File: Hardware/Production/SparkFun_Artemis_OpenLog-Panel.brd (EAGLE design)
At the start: 137.2 x 168.9 mm, 2070 parts, among them J100 CORTEX_JTAG, J107 MICRO-SD, J109 CORTEX_JTAG, J116 MICRO-SD, J118 CORTEX_JTAG, J125 MICRO-SD, J127 CORTEX_JTAG, J134 MICRO-SD, J136 CORTEX_JTAG, J14 CORTEX_JTAG, J143 MICRO-SD, J17 MICRO-SD, J19 CORTEX_JTAG, J26 MICRO-SD, J28 CORTEX_JTAG, J35 MICRO-SD, J37 CORTEX_JTAG, J44 MICRO-SD, J46 CORTEX_JTAG, J53 MICRO-SD, J55 CORTEX_JTAG, J6 MICRO-SD, J62 MICRO-SD, J64 CORTEX_JTAG, J71 MICRO-SD, J73 CORTEX_JTAG, J8 CORTEX_JTAG, J80 MICRO-SD, J82 CORTEX_JTAG, J89 MICRO-SD, J91 CORTEX_JTAG, J98 MICRO-SD, Q1 20V/0.2A/8MHz/1.2Ω/1Vth, Q10 20V/0.2A/8MHz/1.2Ω/1Vth, Q11 20V/0.2A/8MHz/1.2Ω/1Vth, Q12 20V/4.2A/52mΩ/1.4W, Q13 20V/0.2A/8MHz/1.2Ω/1Vth, Q14 20V/0.2A/8MHz/1.2Ω/1Vth, Q15 20V/0.2A/8MHz/1.2Ω/1Vth, Q16 20V/0.2A/8MHz/1.2Ω/1Vth, Q17 20V/0.2A/8MHz/1.2Ω/1Vth, Q18 20V/4.2A/52mΩ/1.4W, Q19 20V/0.2A/8MHz/1.2Ω/1Vth, Q2 20V/4.2A/52mΩ/1.4W, Q20 20V/0.2A/8MHz/1.2Ω/1Vth, Q21 20V/0.2A/8MHz/1.2Ω/1Vth, Q22 20V/0.2A/8MHz/1.2Ω/1Vth, Q23 20V/0.2A/8MHz/1.2Ω/1Vth, Q24 20V/4.2A/52mΩ/1.4W, Q25 20V/0.2A/8MHz/1.2Ω/1Vth, Q26 20V/0.2A/8MHz/1.2Ω/1Vth, Q27 20V/0.2A/8MHz/1.2Ω/1Vth, Q28 20V/0.2A/8MHz/1.2Ω/1Vth, Q29 20V/0.2A/8MHz/1.2Ω/1Vth, Q3 20V/0.2A/8MHz/1.2Ω/1Vth, Q30 20V/4.2A/52mΩ/1.4W, Q31 20V/0.2A/8MHz/1.2Ω/1Vth, Q32 20V/0.2A/8MHz/1.2Ω/1Vth, Q33 20V/0.2A/8MHz/1.2Ω/1Vth, Q34 20V/0.2A/8MHz/1.2Ω/1Vth, Q35 20V/0.2A/8MHz/1.2Ω/1Vth, Q36 20V/4.2A/52mΩ/1.4W, Q37 20V/0.2A/8MHz/1.2Ω/1Vth, Q38 20V/0.2A/8MHz/1.2Ω/1Vth, Q39 20V/0.2A/8MHz/1.2Ω/1Vth, Q4 20V/0.2A/8MHz/1.2Ω/1Vth, Q40 20V/0.2A/8MHz/1.2Ω/1Vth, Q41 20V/0.2A/8MHz/1.2Ω/1Vth, Q42 20V/4.2A/52mΩ/1.4W, Q43 20V/0.2A/8MHz/1.2Ω/1Vth, Q44 20V/0.2A/8MHz/1.2Ω/1Vth, Q45 20V/0.2A/8MHz/1.2Ω/1Vth, Q46 20V/0.2A/8MHz/1.2Ω/1Vth, Q47 20V/0.2A/8MHz/1.2Ω/1Vth, Q48 20V/4.2A/52mΩ/1.4W, Q49 20V/0.2A/8MHz/1.2Ω/1Vth, Q5 20V/0.2A/8MHz/1.2Ω/1Vth, Q50 20V/0.2A/8MHz/1.2Ω/1Vth, Q51 20V/0.2A/8MHz/1.2Ω/1Vth, Q52 20V/0.2A/8MHz/1.2Ω/1Vth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

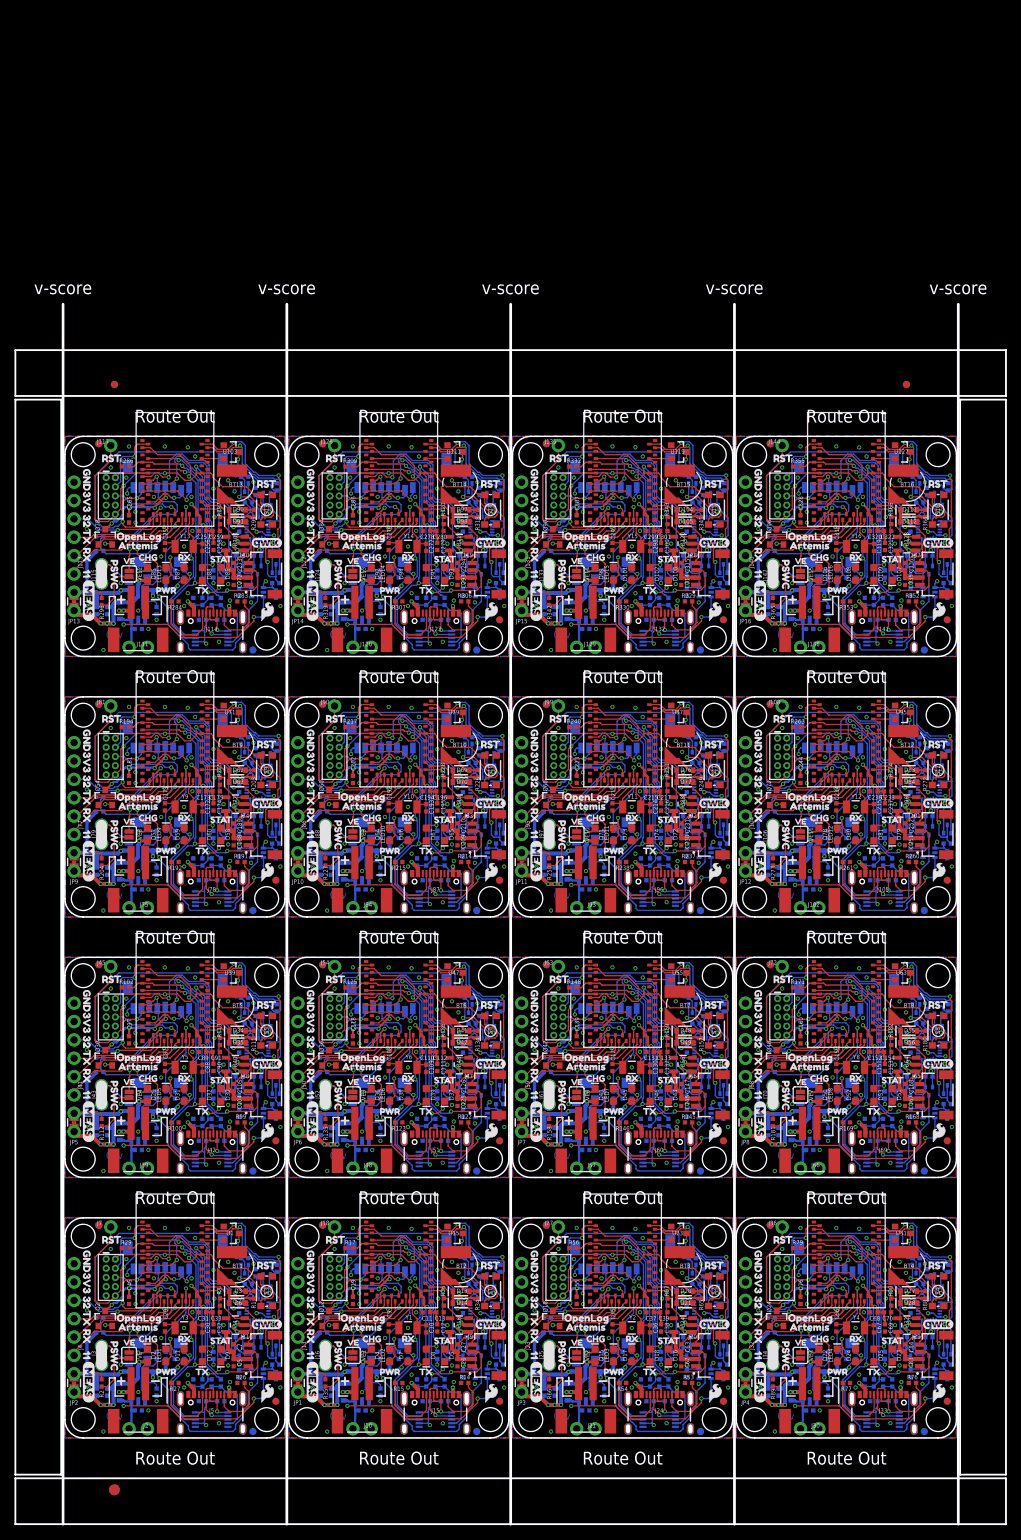
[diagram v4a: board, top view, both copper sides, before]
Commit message: Added revised production files (3x5)
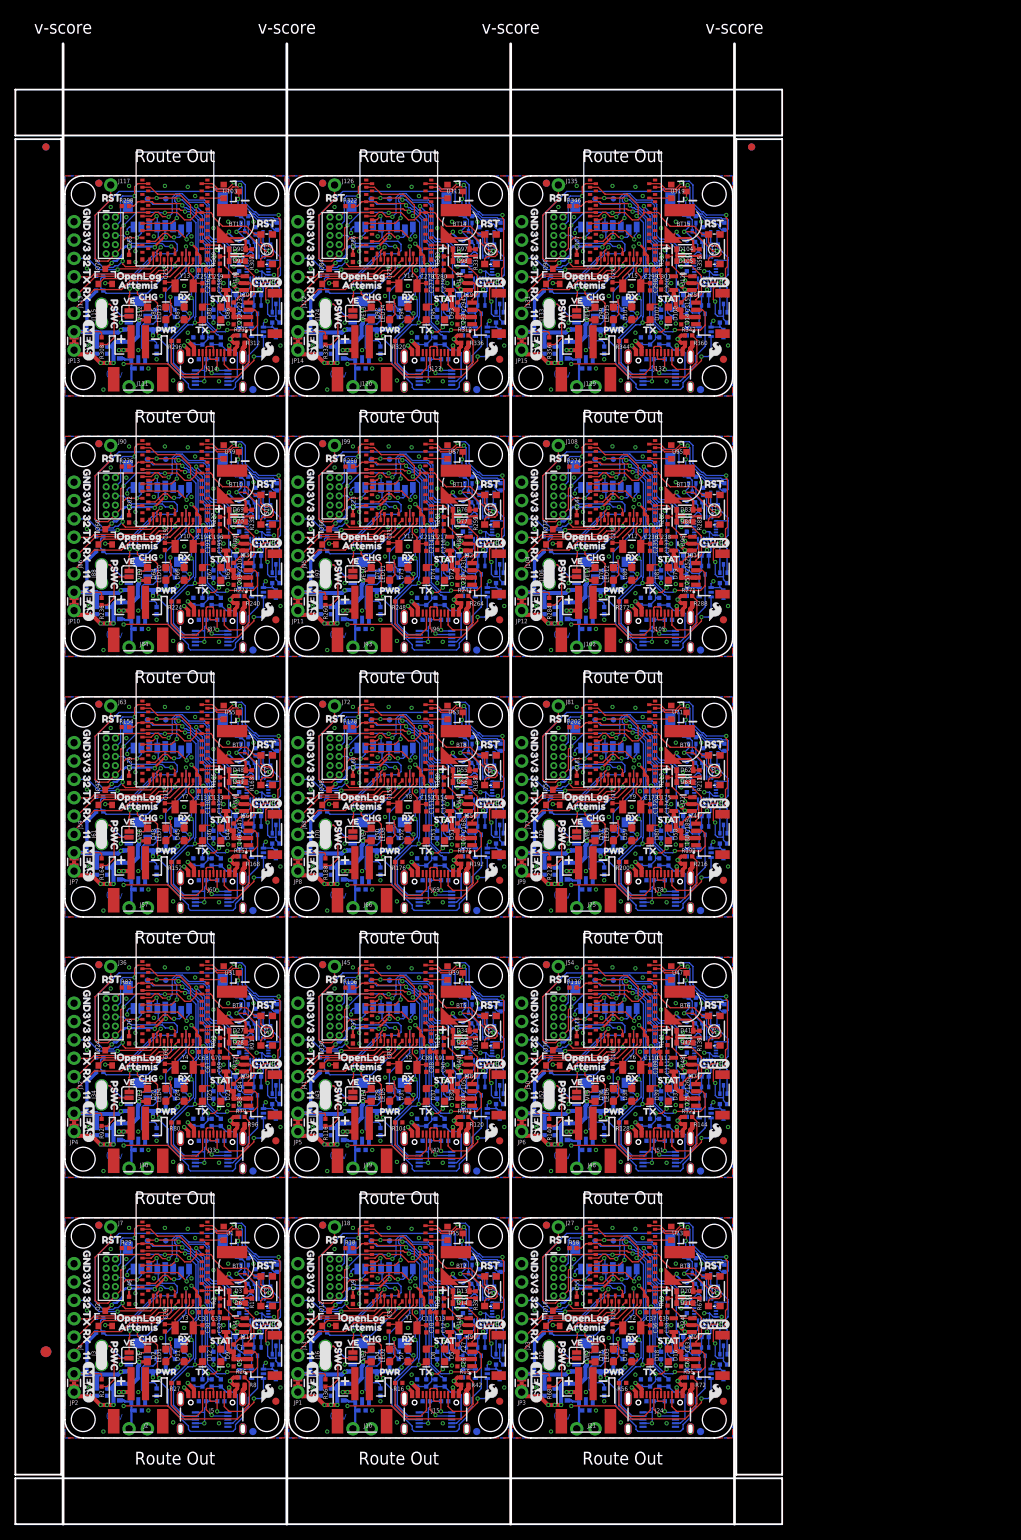
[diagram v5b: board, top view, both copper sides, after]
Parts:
- removed BT16: ML414H, SparkFun-Batteries:ML414H_IV01E
- removed C316, C317: 4.7uF, SparkFun-Capacitors:0402-TIGHT
- removed C318, C319: 15pF, SparkFun-Capacitors:0402-TIGHT
- removed C320, C324, C325, C326, C328, C329, C330, C335: 0.1uF, SparkFun-Capacitors:0402-TIGHT
- removed C321: 10uF, SparkFun-Capacitors:0402-TIGHT
- removed C322, C331, C332, C333: 1.0uF, SparkFun-Capacitors:0402-TIGHT
- removed C323: 10nF, SparkFun-Capacitors:0402-TIGHT
- removed C327: 1.0nF, SparkFun-Capacitors:0402-TIGHT
- removed C334, C336: 2.2uF, SparkFun-Capacitors:0402-TIGHT
- removed D106, D108: Yellow, SparkFun-LED:LED-0603
- removed D107: BLUE, SparkFun-LED:LED-0603
- removed D109: GREEN, SparkFun-LED:LED-0603
- removed D110, D111: 3A/10V/280mV, SparkFun-DiscreteSemi:SOD-323
- removed D112: 1A/23V/620mV, SparkFun-DiscreteSemi:SOD-323
- removed FD61, FD62, FD63, FD64: FIDUCIAL1X2, SparkFun-Aesthetics:FIDUCIAL-1X2
- removed H61, H62, H63, H64: STAND-OFF, SparkFun-Hardware:STAND-OFF
- removed J136: CORTEX_JTAG, SparkFun-Connectors:2X5-PTH-1.27MM
- removed J137: (no value), SparkFun-Connectors:JST04_1MM_RA
- removed J138: (no value), SparkFun-Connectors:JST-2-SMD
- removed J139, J142: (no value), SparkFun-Connectors:1X02_NO_SILK
- removed J140: (no value), SparkFun-Connectors:1X06_NO_SILK
- removed J141: (no value), SparkFun-Connectors:USB-C-16P_4LAYER-PADS
- removed J143: MICRO-SD, SparkFun-Connectors:MICRO-SD-SOCKET
- removed J144: (no value), SparkFun-Connectors:1X01_NO_SILK
- removed JP16: MEAS, SparkFun-Jumpers:COMBO-JUMPER_2_NC_TRACE
- removed LED16: RED, SparkFun-LED:LED-0603
- removed LOGO61: OSHW-LOGOS, SparkFun-Aesthetics:OSHW-LOGO-S
- removed LOGO62, LOGO64: SFE_LOGO_FLAME.1_INCH, SparkFun-Aesthetics:SFE_LOGO_FLAME_.1
- removed LOGO63: SFE_LOGO_NAME.1_INCH, SparkFun-Aesthetics:SFE_LOGO_NAME_.1
- removed Q91, Q92, Q93, Q94, Q95: 20V/0.2A/8MHz/1.2Ω/1Vth, SparkFun-DiscreteSemi:SOT-416FL
- removed Q96: 20V/4.2A/52mΩ/1.4W, SparkFun-DiscreteSemi:SOT23-3
- removed R361, R362: 2.2k, SparkFun-Resistors:0402-TIGHT
- removed R363: DNP, SparkFun-Resistors:0402-TIGHT
- removed R364: 1k, SparkFun-Resistors:0402-TIGHT
- removed R365: 330K, New_Parts:0402-TIGHT
- removed R366: 220k, SparkFun-Resistors:0402-TIGHT
- removed R367: 1M, New_Parts:0402-TIGHT
- removed R368: 2M, New_Parts:0402-TIGHT
- removed S16: RESET, SparkFun-Switches:TACTILE_SWITCH_SMD_4.6X2.8MM
- removed U$586, U$587: (no value), buzzard_labels (14):TX0
- removed U$588, U$589: (no value), buzzard_labels:PSWC0
- removed U$590: (no value), buzzard_labels (19):VE0
- removed U$591, U$592: (no value), RST_04:RST0
- removed U121: MCP73831, SparkFun-IC-Power:SOT23-5
- removed U122: ARTEMIS_MODULE, SparkFun-IC-Microcontroller:ARTEMIS_FP
- removed U123: CH340E, SparkFun-IC-Comms:MSOP10
- removed U124: ICM-20948, SparkFun-Sensors:QFN24-3X3
- removed U125: 1.8V/100mA, SparkFun-IC-Power:SC70
- removed U126, U128: AP2112K, SparkFun-IC-Power:SOT23-5
- removed U127: 3.0V Supervisor, SparkFun-IC-Power:SOT23-3
- removed VE15: (no value), SparkFun-Jumpers:SMT-JUMPER_2_NO_SILK
- removed Y16: 32.768kHz, SparkFun-Clocks:CRYSTAL-SMD-3.2X1.5MM
- added SCL, SCL1, SCL10, SCL11, SCL12, SCL13, SCL14, SCL2, SCL3, SCL4, SCL5, SCL6, SCL7, SCL8, SCL9, SDA, SDA1, SDA10, SDA11, SDA12, SDA13, SDA14, SDA2, SDA3, SDA4, SDA5, SDA6, SDA7, SDA8, SDA9, TP1, TP10, TP11, TP12, TP13, TP14, TP15, TP2, TP3, TP4, TP5, TP6, TP7, TP8, TP9: TEST-POINT3, SparkFun-Connectors:PAD.03X.03
- R100, R122, R123, R14, R146, R283, R307, R53, R54, R76, R77, R99: value 5.1k -> 1k
- R101, R124, R147, R170, R331, R78: value 100k -> 1k
- R102, R125, R148, R171, R194, R355: value 220KOHM-0402T-1/16W-1% -> 1k
- R103, R104, R127, R128, R151, R152, R175, R176, R199, R200, R223, R224, R247, R80: value 2.2k -> 5.1k
- R105, R129, R153, R177, R201, R57, R81: value 2.2k -> 100k
- R106, R130, R154, R178, R18, R346, R58, R82: value 2.2k -> 220KOHM-0402T-1/16W-1%
- R110, R133, R156, R179, R33, R64, R87: value DNP -> 2.2k
- R111, R121, R134, R157, R180, R203, R209, R232, R233, R255, R256, R257, R278, R279, R280, R281, R301, R302, R303, R304, R305, R324, R325, R326, R327, R328, R347, R348, R349, R350, R351, R43, R65, R73, R88, R9, R97: value 1k -> 2.2k
- R112, R135, R158, R181, R204, R227, R89: value 330K -> 2.2k; device New_Parts:0402-TIGHT -> SparkFun-Resistors:0402-TIGHT
- R113, R136, R159, R182, R205, R228, R251: value 220k -> 2.2k
- R114: value 1M -> DNP; device New_Parts:0402-TIGHT -> SparkFun-Resistors:0402-TIGHT
- R115: value 2M -> 1k; device New_Parts:0402-TIGHT -> SparkFun-Resistors:0402-TIGHT
- R116, R356: value 2.2k -> 330K; device SparkFun-Resistors:0402-TIGHT -> New_Parts:0402-TIGHT
- R117, R141, R165, R189, R213: value 1k -> 220k
- R118, R142, R166, R190, R94: value 1k -> 1M; device SparkFun-Resistors:0402-TIGHT -> New_Parts:0402-TIGHT
- R119, R143, R167, R71, R95: value 1k -> 2M; device SparkFun-Resistors:0402-TIGHT -> New_Parts:0402-TIGHT
- R120, R144, R42, R72, R96: value 1k -> 0
- R126, R139, R149, R150, R172, R173, R174, R195, R196, R197, R198, R218, R219, R220, R221, R222, R242, R243, R244, R245, R246, R266, R267, R268, R269, R270, R290, R291, R292, R293, R314, R315, R316, R338, R339: value 2.2k -> 1k
- R137, R160, R183, R206, R229, R252, R275: value 1M -> 2.2k; device New_Parts:0402-TIGHT -> SparkFun-Resistors:0402-TIGHT
- R138: value 2M -> DNP; device New_Parts:0402-TIGHT -> SparkFun-Resistors:0402-TIGHT
- R140, R164, R188, R212, R236: value 1k -> 330K; device SparkFun-Resistors:0402-TIGHT -> New_Parts:0402-TIGHT
- R145, R169, R329, R352, R353: value 5.1k -> 2.2k
- R16, R55: value 100k -> 5.1k
- R161, R184, R207, R230, R253, R276, R299: value 2M -> 2.2k; device New_Parts:0402-TIGHT -> SparkFun-Resistors:0402-TIGHT
- R162: value 2.2k -> DNP
- R168, R192: value 5.1k -> 0
- R17: value 220KOHM-0402T-1/16W-1% -> 100k
- R186, R210, R234, R258, R282, R34: value 1k -> DNP
- R191, R215: value 5.1k -> 2M; device SparkFun-Resistors:0402-TIGHT -> New_Parts:0402-TIGHT
- R193: value 100k -> 2.2k
- R202: value DNP -> 220KOHM-0402T-1/16W-1%
- R214, R238: value 5.1k -> 1M; device SparkFun-Resistors:0402-TIGHT -> New_Parts:0402-TIGHT
- R216: value 100k -> 0
- R217: value 220KOHM-0402T-1/16W-1% -> 2.2k
- R225: value DNP -> 100k
- R226: value 1k -> 220KOHM-0402T-1/16W-1%
- R237, R261: value 5.1k -> 220k
- R239: value 100k -> 2M; device SparkFun-Resistors:0402-TIGHT -> New_Parts:0402-TIGHT
- R240: value 220KOHM-0402T-1/16W-1% -> 0
- R248, R271: value DNP -> 5.1k
- R249: value 1k -> 100k
- R250: value 330K -> 220KOHM-0402T-1/16W-1%; device New_Parts:0402-TIGHT -> SparkFun-Resistors:0402-TIGHT
- R260, R284: value 5.1k -> 330K; device SparkFun-Resistors:0402-TIGHT -> New_Parts:0402-TIGHT
- R262: value 100k -> 1M; device SparkFun-Resistors:0402-TIGHT -> New_Parts:0402-TIGHT
- R263: value 220KOHM-0402T-1/16W-1% -> 2M; device SparkFun-Resistors:0402-TIGHT -> New_Parts:0402-TIGHT
- R264, R288, R312, R336, R360, R8: value 2.2k -> 0
- R272, R295: value 1k -> 5.1k
- R273: value 330K -> 100k; device New_Parts:0402-TIGHT -> SparkFun-Resistors:0402-TIGHT
- R274: value 220k -> 220KOHM-0402T-1/16W-1%
- R285: value 100k -> 220k
- R286: value 220KOHM-0402T-1/16W-1% -> 1M; device SparkFun-Resistors:0402-TIGHT -> New_Parts:0402-TIGHT
- R287, R311, R335, R359, R39: value 2.2k -> 2M; device SparkFun-Resistors:0402-TIGHT -> New_Parts:0402-TIGHT
- R294, R317, R340: value DNP -> 1k
- R296, R319: value 330K -> 5.1k; device New_Parts:0402-TIGHT -> SparkFun-Resistors:0402-TIGHT
- R297: value 220k -> 100k
- R298: value 1M -> 220KOHM-0402T-1/16W-1%; device New_Parts:0402-TIGHT -> SparkFun-Resistors:0402-TIGHT
- R306, R330: value 5.1k -> DNP
- R308: value 100k -> 330K; device SparkFun-Resistors:0402-TIGHT -> New_Parts:0402-TIGHT
- R309: value 220KOHM-0402T-1/16W-1% -> 220k
- R310, R334, R358, R70: value 2.2k -> 1M; device SparkFun-Resistors:0402-TIGHT -> New_Parts:0402-TIGHT
- R320, R343: value 220k -> 5.1k
- R321: value 1M -> 100k; device New_Parts:0402-TIGHT -> SparkFun-Resistors:0402-TIGHT
- R322: value 2M -> 220KOHM-0402T-1/16W-1%; device New_Parts:0402-TIGHT -> SparkFun-Resistors:0402-TIGHT
- R332: value 220KOHM-0402T-1/16W-1% -> 330K; device SparkFun-Resistors:0402-TIGHT -> New_Parts:0402-TIGHT
- R333, R357, R93: value 2.2k -> 220k
- R342, R35: value 330K -> 1k; device New_Parts:0402-TIGHT -> SparkFun-Resistors:0402-TIGHT
- R344: value 1M -> 5.1k; device New_Parts:0402-TIGHT -> SparkFun-Resistors:0402-TIGHT
- R345: value 2M -> 100k; device New_Parts:0402-TIGHT -> SparkFun-Resistors:0402-TIGHT
- R354: value 100k -> DNP
- R36: value 220k -> 330K; device SparkFun-Resistors:0402-TIGHT -> New_Parts:0402-TIGHT
- R37: value 1M -> 220k; device New_Parts:0402-TIGHT -> SparkFun-Resistors:0402-TIGHT
- R38: value 2M -> 1M
- R56, R79: value 220KOHM-0402T-1/16W-1% -> 5.1k
- R66: value 330K -> DNP; device New_Parts:0402-TIGHT -> SparkFun-Resistors:0402-TIGHT
- R67: value 220k -> 1k
- R68: value 1M -> 330K
- R69: value 2M -> 220k; device New_Parts:0402-TIGHT -> SparkFun-Resistors:0402-TIGHT
- R90: value 220k -> DNP
- R91: value 1M -> 1k; device New_Parts:0402-TIGHT -> SparkFun-Resistors:0402-TIGHT
- R92: value 2M -> 330K
- U$100, U$99: device buzzard_labels (14):322 -> buzzard_labels (14):3V34
- U$101, U$102: device buzzard_labels (14):GND5 -> buzzard_labels (14):113
- U$103, U$104: device buzzard_labels (14):RX1 -> buzzard_labels (14):322
- U$105, U$106: device buzzard_labels (14):TX0 -> buzzard_labels (14):GND5
- U$107, U$108: device buzzard_labels:PSWC0 -> buzzard_labels (14):RX1
- U$109: device buzzard_labels (19):VE0 -> buzzard_labels (14):TX0
- U$110, U$148: device RST_04:RST0 -> buzzard_labels (14):TX0
- U$111, U$73: device RST_04:RST0 -> buzzard_labels:PSWC0
- U$112: device buzzard_labels (2):MEAS3 -> buzzard_labels:PSWC0
- U$113, U$230: device buzzard_labels (1):X0 -> buzzard_labels (19):VE0
- U$114, U$231: device buzzard_labels (1):Y1 -> RST_04:RST0
- U$115, U$232: device buzzard_labels (1):Z2 -> RST_04:RST0
- U$116: device buzzard_labels (1):G5 -> output:C0
- U$117: device buzzard_labels (1):A4 -> output:D0
- U$118: device buzzard_labels (1):M3 -> buzzard_labels (2):MEAS3
- U$122: device qwiic#logo#jpg:QWIIC#LOGO#JPG -> buzzard_labels (1):G5
- U$123: device buzzard_labels (12):CHG2 -> buzzard_labels (1):A4
- U$124: device buzzard_labels (12):PWR0 -> buzzard_labels (1):M3
- U$125, U$236: device buzzard_labels (12):RX4 -> buzzard_labels (1):X0
- U$126, U$237: device buzzard_labels (12):STAT5 -> buzzard_labels (1):Y1
- U$127, U$238: device buzzard_labels (12):TX3 -> buzzard_labels (1):Z2
- U$128: device buzzard_labels (13):ARTEMIS13 -> qwiic#logo#jpg:QWIIC#LOGO#JPG
- U$129: device buzzard_labels (13):OPENLOG12 -> buzzard_labels (12):CHG2
- U$13: device buzzard_labels (2):MEAS3 -> output:C0
- U$130: device buzzard_labels (13):RST9 -> buzzard_labels (12):PWR0
- U$131: device buzzard_labels (13):VIN8 -> buzzard_labels (12):RX4
- U$132: device buzzard_labels (14):3V34 -> buzzard_labels (12):STAT5
- U$133: device buzzard_labels (14):3V34 -> buzzard_labels (12):TX3
- U$134: device buzzard_labels (14):113 -> buzzard_labels (13):ARTEMIS13
- U$135: device buzzard_labels (14):113 -> buzzard_labels (13):OPENLOG12
- U$136: device buzzard_labels (14):322 -> buzzard_labels (13):RST9
- U$137: device buzzard_labels (14):322 -> buzzard_labels (13):VIN8
- U$138, U$139: device buzzard_labels (14):GND5 -> buzzard_labels (14):3V34
- U$14, U$156: device buzzard_labels (1):X0 -> output:D0
- U$140, U$141: device buzzard_labels (14):RX1 -> buzzard_labels (14):113
- U$142, U$143: device buzzard_labels (14):TX0 -> buzzard_labels (14):322
- U$144, U$145: device buzzard_labels:PSWC0 -> buzzard_labels (14):GND5
- U$146: device buzzard_labels (19):VE0 -> buzzard_labels (14):RX1
- U$147, U$185: device RST_04:RST0 -> buzzard_labels (14):RX1
- U$149: device buzzard_labels (2):MEAS3 -> buzzard_labels (14):TX0
- U$15, U$157: device buzzard_labels (1):Y1 -> buzzard_labels (2):MEAS3
- U$150, U$267: device buzzard_labels (1):X0 -> buzzard_labels:PSWC0
- U$151, U$268: device buzzard_labels (1):Y1 -> buzzard_labels:PSWC0
- U$152, U$269: device buzzard_labels (1):Z2 -> buzzard_labels (19):VE0
- U$153: device buzzard_labels (1):G5 -> RST_04:RST0
- U$154: device buzzard_labels (1):A4 -> RST_04:RST0
- U$155: device buzzard_labels (1):M3 -> output:C0
- U$158, U$16, U$22: device buzzard_labels (1):Z2 -> buzzard_labels (1):X0
- U$159, U$23: device qwiic#logo#jpg:QWIIC#LOGO#JPG -> buzzard_labels (1):Y1
- U$160, U$24: device buzzard_labels (12):CHG2 -> buzzard_labels (1):Z2
- U$161: device buzzard_labels (12):PWR0 -> buzzard_labels (1):G5
- U$162: device buzzard_labels (12):RX4 -> buzzard_labels (1):A4
- U$163: device buzzard_labels (12):STAT5 -> buzzard_labels (1):M3
- U$164, U$275: device buzzard_labels (12):TX3 -> buzzard_labels (1):X0
- U$165, U$276: device buzzard_labels (13):ARTEMIS13 -> buzzard_labels (1):Y1
- U$166, U$277: device buzzard_labels (13):OPENLOG12 -> buzzard_labels (1):Z2
- U$167: device buzzard_labels (13):RST9 -> qwiic#logo#jpg:QWIIC#LOGO#JPG
- U$168: device buzzard_labels (13):VIN8 -> buzzard_labels (12):CHG2
- U$169: device buzzard_labels (14):3V34 -> buzzard_labels (12):PWR0
- U$17: device buzzard_labels (1):G5 -> buzzard_labels (1):Y1
- U$170: device buzzard_labels (14):3V34 -> buzzard_labels (12):RX4
- U$171: device buzzard_labels (14):113 -> buzzard_labels (12):STAT5
- U$172: device buzzard_labels (14):113 -> buzzard_labels (12):TX3
- U$173: device buzzard_labels (14):322 -> buzzard_labels (13):ARTEMIS13
- U$174: device buzzard_labels (14):322 -> buzzard_labels (13):OPENLOG12
- U$175: device buzzard_labels (14):GND5 -> buzzard_labels (13):RST9
- U$176: device buzzard_labels (14):GND5 -> buzzard_labels (13):VIN8
- U$177, U$178: device buzzard_labels (14):RX1 -> buzzard_labels (14):3V34
- U$179, U$180: device buzzard_labels (14):TX0 -> buzzard_labels (14):113
- U$18: device buzzard_labels (1):A4 -> buzzard_labels (1):Z2
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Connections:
- removed net !POWER_LOSS!15: U122.D3, U127.2
- removed net 3.3V15: C323.1, C324.1, C332.1, C334.1, D112.A, J136.1, J140.5, Q96.2, R350.2, R351.2, R359.2, R361.2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
- removed net 5V15: C317.1, D106.A, D110.C, J141.VBUS1, J141.VBUS2, JP16.1, JP16.3, U121.4
- removed net ARTEMIS_!RESET15: C325.2, C327.1, J136.10, J144.1, R354.1, S16.3, S16.4, U122.~RST
- removed net ARTEMIS_!RTS!15: C325.1, C326.1, U123.4
- removed net ARTEMIS_BOOT15: C326.2, R355.2, U122.BOOT
- removed net ARTEMIS_RX15: D108.C, U122.RXI-0, U123.8
- removed net ARTEMIS_SWDCK15: J136.4, U122.SWDCK
- removed net ARTEMIS_SWDIO15: J136.2, U122.SWDIO
- removed net ARTEMIS_TX15: D109.C, U122.TXO-0, U123.9
- removed net ARTEMIS_~AD12/TX16: J140.3, U122.~AD12
- removed net ARTEMIS_~AD13/RX16: J140.2, U122.~AD13
- removed net ARTEMIS_~AD30: J140.1, U122.~AD11
- removed net ARTEMIS_~AD31: J140.4, U122.~AD32
- removed net CC31: J141.B5, R352.2
- removed net CC32: J141.A5, R353.2
- removed net CHG_LED15: R347.1, U121.1
- removed net D+16: J141.A6, J141.B6, U123.1
- removed net D-16: J141.A7, J141.B7, U123.2
- removed net DAT31: J143.RSV2, U122.~D26
- removed net DAT32: J143.RSV1, U122.~D4
- removed net GND15: BT16.-, C316.2, C317.2, C318.1, C319.1, C320.1, C321.2, C322.2, C323.2, C324.2, C327.2, C328.2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
- removed net ICM-20948-LV_!CS!15: Q94.2, R360.1, U124.22
- removed net ICM-20948-LV_#_1.8V15: C330.1, C331.1, Q91.1, Q92.1, Q93.1, Q94.1, Q95.1, R356.2, R357.2, R358.2, R360.2, R362.2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
- removed net ICM-20948-LV_INT15: Q93.2, R358.1, U124.12
- removed net ICM-20948-LV_MISO15: Q95.2, R362.1, U124.9
- removed net ICM-20948-LV_MOSI15: Q92.2, R357.1, U124.24
- removed net ICM-20948-LV_SCK15: Q91.2, R356.1, U124.23
- removed net ICM_!CS!15: Q94.3, R361.1, U122.~D44
- removed net ICM_INT15: Q93.3, R359.1, U122.~D37
- removed net ICM_PWR15: U122.~D27, U125.3
- removed net MICROSD_!CS!15: J143.CS, U122.~D23
- removed net MICROSD_PWR15: Q96.1, U122.D15
- removed net MISO15: J143.DO, Q95.3, R363.1, U122.~D22, U122.~D6
- removed net MOSI15: J143.DI, Q92.3, U122.D7
- removed net N$151: R346.2, U121.5
- removed net N$152: D106.C, R347.2
- removed net N$153: C318.2, U122.XO, Y16.P$2
- removed net N$154: C319.2, U122.XI, Y16.P$1
- removed net N$155: LED16.A, R348.1
- removed net N$156: D107.A, R349.1
- removed net N$157: D109.A, R351.1
- removed net N$158: D108.A, R350.1
- removed net N$159: C329.1, U124.10
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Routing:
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- removed copper zone on layer 15, net 3.3V15
- removed copper zone on layer 15, net 5V15
- removed copper zone on layer 1, net GND15
- removed copper zone on layer 16, net GND15
- removed copper zone on layer 2, net GND15
- removed copper zone on layer 15, net VIN15
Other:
- board size 137.2 x 168.9 mm -> 106.2 x 205 mm

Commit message: Final V10 PCB tweaks!?
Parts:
- added GND, GND1, GND10, GND11, GND12, GND13, GND14, GND2, GND3, GND4, GND5, GND6, GND7, GND8, GND9, QWIIC_3.3V, QWIIC_3.3V1, QWIIC_3.3V10, QWIIC_3.3V11, QWIIC_3.3V12, QWIIC_3.3V13, QWIIC_3.3V14, QWIIC_3.3V2, QWIIC_3.3V3, QWIIC_3.3V4, QWIIC_3.3V5, QWIIC_3.3V6, QWIIC_3.3V7, QWIIC_3.3V8, QWIIC_3.3V9: TEST-POINTTP_15TH_THRU, SparkFun-Connectors:TP_15TH
- added U$586: (no value), buzzard_labels (14):322
- added U$587, U$588: (no value), buzzard_labels (14):GND5
- added U$589, U$590: (no value), buzzard_labels (14):RX1
- added U$591, U$592: (no value), buzzard_labels (14):TX0
- added U$593, U$594: (no value), buzzard_labels:PSWC0
- added U$595: (no value), buzzard_labels (19):VE0
- added U$596, U$597: (no value), RST_04:RST0
- added U$598: (no value), output:C0
- added U$599: (no value), output:D0
- added U$600: (no value), output:30
- SCL, SCL1, SCL10, SCL11, SCL12, SCL13, SCL14, SCL2, SCL3, SCL4, SCL5, SCL6, SCL7, SCL8, SCL9, SDA, SDA1, SDA10, SDA11, SDA12, SDA13, SDA14, SDA2, SDA3, SDA4, SDA5, SDA6, SDA7, SDA8, SDA9: value TEST-POINT3 -> TEST-POINTTP_15TH_THRU; device SparkFun-Connectors:PAD.03X.03 -> SparkFun-Connectors:TP_15TH
- U$100, U$60: device buzzard_labels (14):3V34 -> buzzard_labels (13):VIN8
- U$101, U$102, U$141, U$62: device buzzard_labels (14):113 -> buzzard_labels (14):3V34
- U$103, U$104, U$143, U$64: device buzzard_labels (14):322 -> buzzard_labels (14):113
- U$105, U$106, U$145, U$66: device buzzard_labels (14):GND5 -> buzzard_labels (14):322
- U$107, U$108, U$147, U$68: device buzzard_labels (14):RX1 -> buzzard_labels (14):GND5
- U$109, U$110, U$149, U$70: device buzzard_labels (14):TX0 -> buzzard_labels (14):RX1
- U$111, U$112, U$151, U$72: device buzzard_labels:PSWC0 -> buzzard_labels (14):TX0
- U$113, U$74: device buzzard_labels (19):VE0 -> buzzard_labels:PSWC0
- U$114, U$153, U$154, U$193: device RST_04:RST0 -> buzzard_labels:PSWC0
- U$115, U$75: device RST_04:RST0 -> buzzard_labels (19):VE0
- U$116, U$77: device output:C0 -> RST_04:RST0
- U$117, U$156: device output:D0 -> RST_04:RST0
- U$118: device buzzard_labels (2):MEAS3 -> output:C0
- U$119, U$359: device buzzard_labels (1):X0 -> output:D0
- U$120, U$360: device buzzard_labels (1):Y1 -> output:30
- U$121, U$361: device buzzard_labels (1):Z2 -> buzzard_labels (2):MEAS3
- U$122: device buzzard_labels (1):G5 -> buzzard_labels (1):X0
- U$123: device buzzard_labels (1):A4 -> buzzard_labels (1):Y1
- U$124: device buzzard_labels (1):M3 -> buzzard_labels (1):Z2
- U$125: device buzzard_labels (1):X0 -> buzzard_labels (1):G5
- U$126: device buzzard_labels (1):Y1 -> buzzard_labels (1):A4
- U$127: device buzzard_labels (1):Z2 -> buzzard_labels (1):M3
- U$128, U$362: device qwiic#logo#jpg:QWIIC#LOGO#JPG -> buzzard_labels (1):X0
- U$129, U$363: device buzzard_labels (12):CHG2 -> buzzard_labels (1):Y1
- U$130, U$364: device buzzard_labels (12):PWR0 -> buzzard_labels (1):Z2
- U$131: device buzzard_labels (12):RX4 -> qwiic#logo#jpg:QWIIC#LOGO#JPG
- U$132: device buzzard_labels (12):STAT5 -> buzzard_labels (12):CHG2
- U$133: device buzzard_labels (12):TX3 -> buzzard_labels (12):PWR0
- U$134: device buzzard_labels (13):ARTEMIS13 -> buzzard_labels (12):RX4
- U$135: device buzzard_labels (13):OPENLOG12 -> buzzard_labels (12):STAT5
- U$136: device buzzard_labels (13):RST9 -> buzzard_labels (12):TX3
- U$137: device buzzard_labels (13):VIN8 -> buzzard_labels (13):ARTEMIS13
- U$138, U$178: device buzzard_labels (14):3V34 -> buzzard_labels (13):OPENLOG12
- U$139, U$99: device buzzard_labels (14):3V34 -> buzzard_labels (13):RST9
- U$140, U$180: device buzzard_labels (14):113 -> buzzard_labels (13):VIN8
- U$142, U$181, U$182, U$221: device buzzard_labels (14):322 -> buzzard_labels (14):3V34
- U$144, U$183, U$184, U$223: device buzzard_labels (14):GND5 -> buzzard_labels (14):113
- U$146, U$185, U$186, U$225: device buzzard_labels (14):RX1 -> buzzard_labels (14):322
- U$148, U$187, U$188, U$227: device buzzard_labels (14):TX0 -> buzzard_labels (14):GND5
- U$15: device buzzard_labels (2):MEAS3 -> output:30
- U$150, U$189, U$190, U$229: device buzzard_labels:PSWC0 -> buzzard_labels (14):RX1
- U$152, U$191: device buzzard_labels (19):VE0 -> buzzard_labels (14):TX0
- U$155: device output:C0 -> buzzard_labels (19):VE0
- U$157, U$196: device buzzard_labels (2):MEAS3 -> RST_04:RST0
- U$158, U$398: device buzzard_labels (1):X0 -> output:C0
- U$159, U$399: device buzzard_labels (1):Y1 -> output:D0
- U$16, U$281: device buzzard_labels (1):X0 -> buzzard_labels (2):MEAS3
- U$160, U$400: device buzzard_labels (1):Z2 -> output:30
- U$161: device buzzard_labels (1):G5 -> buzzard_labels (2):MEAS3
- U$162: device buzzard_labels (1):A4 -> buzzard_labels (1):X0
- U$163: device buzzard_labels (1):M3 -> buzzard_labels (1):Y1
- U$164: device buzzard_labels (1):X0 -> buzzard_labels (1):Z2
- U$165: device buzzard_labels (1):Y1 -> buzzard_labels (1):G5
- U$166: device buzzard_labels (1):Z2 -> buzzard_labels (1):A4
- U$167: device qwiic#logo#jpg:QWIIC#LOGO#JPG -> buzzard_labels (1):M3
- U$168, U$402: device buzzard_labels (12):CHG2 -> buzzard_labels (1):X0
- U$169, U$403: device buzzard_labels (12):PWR0 -> buzzard_labels (1):Y1
- U$17, U$23, U$282: device buzzard_labels (1):Y1 -> buzzard_labels (1):X0
- U$170, U$404: device buzzard_labels (12):RX4 -> buzzard_labels (1):Z2
- U$171: device buzzard_labels (12):STAT5 -> qwiic#logo#jpg:QWIIC#LOGO#JPG
- U$172: device buzzard_labels (12):TX3 -> buzzard_labels (12):CHG2
- U$173: device buzzard_labels (13):ARTEMIS13 -> buzzard_labels (12):PWR0
- U$174: device buzzard_labels (13):OPENLOG12 -> buzzard_labels (12):RX4
- U$175: device buzzard_labels (13):RST9 -> buzzard_labels (12):STAT5
- U$176: device buzzard_labels (13):VIN8 -> buzzard_labels (12):TX3
- U$177, U$217: device buzzard_labels (14):3V34 -> buzzard_labels (13):ARTEMIS13
- U$179, U$219: device buzzard_labels (14):113 -> buzzard_labels (13):RST9
- U$18, U$24, U$283: device buzzard_labels (1):Z2 -> buzzard_labels (1):Y1
- U$19: device buzzard_labels (1):G5 -> buzzard_labels (1):Z2
- U$192, U$231, U$232, U$271: device RST_04:RST0 -> buzzard_labels (14):TX0
- U$194, U$233: device output:C0 -> buzzard_labels:PSWC0
- U$195: device output:D0 -> buzzard_labels (19):VE0
- U$197, U$236, U$437, U$476: device buzzard_labels (1):X0 -> RST_04:RST0
- U$198, U$438: device buzzard_labels (1):Y1 -> output:C0
- U$199, U$439: device buzzard_labels (1):Z2 -> output:D0
- U$20: device buzzard_labels (1):A4 -> buzzard_labels (1):G5
- U$200: device buzzard_labels (1):G5 -> output:30
- U$201: device buzzard_labels (1):A4 -> buzzard_labels (2):MEAS3
- U$202: device buzzard_labels (1):M3 -> buzzard_labels (1):X0
- U$203: device buzzard_labels (1):X0 -> buzzard_labels (1):Y1
- U$204: device buzzard_labels (1):Y1 -> buzzard_labels (1):Z2
- U$205: device buzzard_labels (1):Z2 -> buzzard_labels (1):G5
- U$206: device qwiic#logo#jpg:QWIIC#LOGO#JPG -> buzzard_labels (1):A4
- U$207: device buzzard_labels (12):CHG2 -> buzzard_labels (1):M3
- U$208, U$442: device buzzard_labels (12):PWR0 -> buzzard_labels (1):X0
- U$209, U$443: device buzzard_labels (12):RX4 -> buzzard_labels (1):Y1
- U$21: device buzzard_labels (1):M3 -> buzzard_labels (1):A4
- U$210, U$444: device buzzard_labels (12):STAT5 -> buzzard_labels (1):Z2
- U$211: device buzzard_labels (12):TX3 -> qwiic#logo#jpg:QWIIC#LOGO#JPG
- U$212: device buzzard_labels (13):ARTEMIS13 -> buzzard_labels (12):CHG2
- U$213: device buzzard_labels (13):OPENLOG12 -> buzzard_labels (12):PWR0
- U$214: device buzzard_labels (13):RST9 -> buzzard_labels (12):RX4
- U$215: device buzzard_labels (13):VIN8 -> buzzard_labels (12):STAT5
- U$216, U$256: device buzzard_labels (14):3V34 -> buzzard_labels (12):TX3
- U$218, U$258: device buzzard_labels (14):113 -> buzzard_labels (13):OPENLOG12
- U$22: device buzzard_labels (1):X0 -> buzzard_labels (1):M3
- U$220, U$260: device buzzard_labels (14):322 -> buzzard_labels (13):VIN8
- U$222, U$261, U$262, U$301: device buzzard_labels (14):GND5 -> buzzard_labels (14):3V34
- U$224, U$263, U$264, U$303: device buzzard_labels (14):RX1 -> buzzard_labels (14):113
- U$226, U$265, U$266, U$305: device buzzard_labels (14):TX0 -> buzzard_labels (14):322
- U$228, U$267, U$268, U$307: device buzzard_labels:PSWC0 -> buzzard_labels (14):GND5
- U$230, U$269: device buzzard_labels (19):VE0 -> buzzard_labels (14):RX1
- U$234, U$273: device output:D0 -> buzzard_labels:PSWC0
- U$235: device buzzard_labels (2):MEAS3 -> buzzard_labels (19):VE0
- U$237, U$276, U$477, U$516: device buzzard_labels (1):Y1 -> RST_04:RST0
- U$238, U$478: device buzzard_labels (1):Z2 -> output:C0
- U$239: device buzzard_labels (1):G5 -> output:D0
- U$240: device buzzard_labels (1):A4 -> output:30
- U$241: device buzzard_labels (1):M3 -> buzzard_labels (2):MEAS3
- U$245: device qwiic#logo#jpg:QWIIC#LOGO#JPG -> buzzard_labels (1):G5
- U$246: device buzzard_labels (12):CHG2 -> buzzard_labels (1):A4
- U$247: device buzzard_labels (12):PWR0 -> buzzard_labels (1):M3
- U$248, U$482: device buzzard_labels (12):RX4 -> buzzard_labels (1):X0
- U$249, U$483: device buzzard_labels (12):STAT5 -> buzzard_labels (1):Y1
- U$25, U$284: device qwiic#logo#jpg:QWIIC#LOGO#JPG -> buzzard_labels (1):Z2
- U$250, U$484: device buzzard_labels (12):TX3 -> buzzard_labels (1):Z2
- U$251: device buzzard_labels (13):ARTEMIS13 -> qwiic#logo#jpg:QWIIC#LOGO#JPG
- U$252: device buzzard_labels (13):OPENLOG12 -> buzzard_labels (12):CHG2
- U$253: device buzzard_labels (13):RST9 -> buzzard_labels (12):PWR0
- U$254: device buzzard_labels (13):VIN8 -> buzzard_labels (12):RX4
- U$255, U$295: device buzzard_labels (14):3V34 -> buzzard_labels (12):STAT5
- U$257, U$297: device buzzard_labels (14):113 -> buzzard_labels (13):ARTEMIS13
- U$259, U$299: device buzzard_labels (14):322 -> buzzard_labels (13):RST9
- U$26: device buzzard_labels (12):CHG2 -> qwiic#logo#jpg:QWIIC#LOGO#JPG
- U$270, U$309, U$310, U$349: device RST_04:RST0 -> buzzard_labels (14):RX1
- U$272, U$311: device output:C0 -> buzzard_labels (14):TX0
- U$274, U$313: device buzzard_labels (2):MEAS3 -> buzzard_labels:PSWC0
- U$275, U$515: device buzzard_labels (1):X0 -> buzzard_labels (19):VE0
- U$277, U$316, U$517, U$556: device buzzard_labels (1):Z2 -> RST_04:RST0
- U$278: device buzzard_labels (1):G5 -> output:C0
- U$279: device buzzard_labels (1):A4 -> output:D0
- U$280: device buzzard_labels (1):M3 -> output:30
- U$285: device buzzard_labels (12):CHG2 -> buzzard_labels (1):G5
- U$286: device buzzard_labels (12):PWR0 -> buzzard_labels (1):A4
- U$287: device buzzard_labels (12):RX4 -> buzzard_labels (1):M3
- U$288, U$522: device buzzard_labels (12):STAT5 -> buzzard_labels (1):X0
- U$289, U$523: device buzzard_labels (12):TX3 -> buzzard_labels (1):Y1
- U$29: device buzzard_labels (12):PWR0 -> buzzard_labels (12):CHG2
- U$290, U$524: device buzzard_labels (13):ARTEMIS13 -> buzzard_labels (1):Z2
- U$291: device buzzard_labels (13):OPENLOG12 -> qwiic#logo#jpg:QWIIC#LOGO#JPG
- U$292: device buzzard_labels (13):RST9 -> buzzard_labels (12):CHG2
- U$293: device buzzard_labels (13):VIN8 -> buzzard_labels (12):PWR0
- U$294, U$334: device buzzard_labels (14):3V34 -> buzzard_labels (12):RX4
- U$296, U$336: device buzzard_labels (14):113 -> buzzard_labels (12):TX3
- U$298, U$338: device buzzard_labels (14):322 -> buzzard_labels (13):OPENLOG12
- U$30: device buzzard_labels (12):RX4 -> buzzard_labels (12):PWR0
- U$300, U$340: device buzzard_labels (14):GND5 -> buzzard_labels (13):VIN8
- U$302, U$341, U$342, U$381: device buzzard_labels (14):RX1 -> buzzard_labels (14):3V34
- U$304, U$343, U$344, U$383: device buzzard_labels (14):TX0 -> buzzard_labels (14):113
- U$306, U$345, U$346, U$385: device buzzard_labels:PSWC0 -> buzzard_labels (14):322
- U$308, U$347: device buzzard_labels (19):VE0 -> buzzard_labels (14):GND5
- U$31: device buzzard_labels (12):STAT5 -> buzzard_labels (12):RX4
- U$312, U$351: device output:D0 -> buzzard_labels (14):TX0
- U$314, U$353, U$554: device buzzard_labels (1):X0 -> buzzard_labels:PSWC0
- U$315, U$555: device buzzard_labels (1):Y1 -> buzzard_labels (19):VE0
- U$317, U$356: device buzzard_labels (1):G5 -> RST_04:RST0
- U$318: device buzzard_labels (1):A4 -> output:C0
- U$319: device buzzard_labels (1):M3 -> output:D0
- U$320, U$80: device buzzard_labels (1):X0 -> output:30
- U$321, U$81: device buzzard_labels (1):Y1 -> buzzard_labels (2):MEAS3
- U$322, U$82, U$88: device buzzard_labels (1):Z2 -> buzzard_labels (1):X0
- U$323, U$89: device qwiic#logo#jpg:QWIIC#LOGO#JPG -> buzzard_labels (1):Y1
- U$324, U$90: device buzzard_labels (12):CHG2 -> buzzard_labels (1):Z2
- U$325: device buzzard_labels (12):PWR0 -> buzzard_labels (1):G5
- U$326: device buzzard_labels (12):RX4 -> buzzard_labels (1):A4
- U$327: device buzzard_labels (12):STAT5 -> buzzard_labels (1):M3
- U$328, U$562: device buzzard_labels (12):TX3 -> buzzard_labels (1):X0
- U$329, U$563: device buzzard_labels (13):ARTEMIS13 -> buzzard_labels (1):Y1
- U$330, U$564: device buzzard_labels (13):OPENLOG12 -> buzzard_labels (1):Z2
- U$331: device buzzard_labels (13):RST9 -> qwiic#logo#jpg:QWIIC#LOGO#JPG
- U$332: device buzzard_labels (13):VIN8 -> buzzard_labels (12):CHG2
- U$333, U$373: device buzzard_labels (14):3V34 -> buzzard_labels (12):PWR0
- U$335, U$375: device buzzard_labels (14):113 -> buzzard_labels (12):STAT5
- U$337, U$377: device buzzard_labels (14):322 -> buzzard_labels (13):ARTEMIS13
- U$339, U$379: device buzzard_labels (14):GND5 -> buzzard_labels (13):RST9
- U$348, U$387, U$388, U$427: device RST_04:RST0 -> buzzard_labels (14):GND5
- U$350, U$389: device output:C0 -> buzzard_labels (14):RX1
- U$352, U$391: device buzzard_labels (2):MEAS3 -> buzzard_labels (14):TX0
- U$354, U$393: device buzzard_labels (1):Y1 -> buzzard_labels:PSWC0
- U$355: device buzzard_labels (1):Z2 -> buzzard_labels (19):VE0
- U$357, U$396: device buzzard_labels (1):A4 -> RST_04:RST0
- U$358: device buzzard_labels (1):M3 -> output:C0
- U$365: device buzzard_labels (12):RX4 -> buzzard_labels (1):G5
- U$366: device buzzard_labels (12):STAT5 -> buzzard_labels (1):A4
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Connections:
- net ICM-20948-LV_MISO renamed ICM-20948-LV_SDO
- net ICM-20948-LV_MISO1 renamed ICM-20948-LV_SDO1
- net ICM-20948-LV_MISO10 renamed ICM-20948-LV_SDO10
- net ICM-20948-LV_MISO11 renamed ICM-20948-LV_SDO11
- net ICM-20948-LV_MISO12 renamed ICM-20948-LV_SDO12
- net ICM-20948-LV_MISO13 renamed ICM-20948-LV_SDO13
- net ICM-20948-LV_MISO14 renamed ICM-20948-LV_SDO14
- net ICM-20948-LV_MISO2 renamed ICM-20948-LV_SDO2
- net ICM-20948-LV_MISO3 renamed ICM-20948-LV_SDO3
- net ICM-20948-LV_MISO4 renamed ICM-20948-LV_SDO4
- net ICM-20948-LV_MISO5 renamed ICM-20948-LV_SDO5
- net ICM-20948-LV_MISO6 renamed ICM-20948-LV_SDO6
- net ICM-20948-LV_MISO7 renamed ICM-20948-LV_SDO7
- net ICM-20948-LV_MISO8 renamed ICM-20948-LV_SDO8
- net ICM-20948-LV_MISO9 renamed ICM-20948-LV_SDO9
- net ICM-20948-LV_MOSI renamed ICM-20948-LV_SDI
- net ICM-20948-LV_MOSI1 renamed ICM-20948-LV_SDI1
- net ICM-20948-LV_MOSI10 renamed ICM-20948-LV_SDI10
- net ICM-20948-LV_MOSI11 renamed ICM-20948-LV_SDI11
- net ICM-20948-LV_MOSI12 renamed ICM-20948-LV_SDI12
- net ICM-20948-LV_MOSI13 renamed ICM-20948-LV_SDI13
- net ICM-20948-LV_MOSI14 renamed ICM-20948-LV_SDI14
- net ICM-20948-LV_MOSI2 renamed ICM-20948-LV_SDI2
- net ICM-20948-LV_MOSI3 renamed ICM-20948-LV_SDI3
- net ICM-20948-LV_MOSI4 renamed ICM-20948-LV_SDI4
- net ICM-20948-LV_MOSI5 renamed ICM-20948-LV_SDI5
- net ICM-20948-LV_MOSI6 renamed ICM-20948-LV_SDI6
- net ICM-20948-LV_MOSI7 renamed ICM-20948-LV_SDI7
- net ICM-20948-LV_MOSI8 renamed ICM-20948-LV_SDI8
- net ICM-20948-LV_MOSI9 renamed ICM-20948-LV_SDI9
- removed net MISO: J6.DO, Q10.3, R49.1, U8.~D22, U8.~D6
- removed net MISO1: J17.DO, Q11.3, R34.1, U6.~D22, U6.~D6
- removed net MISO10: J98.DO, Q65.3, R258.1, U82.~D22, U82.~D6
- removed net MISO11: J107.DO, Q71.3, R282.1, U90.~D22, U90.~D6
- removed net MISO12: J116.DO, Q77.3, R306.1, U98.~D22, U98.~D6
- removed net MISO13: J125.DO, Q83.3, R330.1, U106.~D22, U106.~D6
- removed net MISO14: J134.DO, Q89.3, R354.1, U114.~D22, U114.~D6
- removed net MISO2: J26.DO, Q17.3, R66.1, U18.~D22, U18.~D6
- removed net MISO3: J35.DO, Q23.3, R90.1, U26.~D22, U26.~D6
- removed net MISO4: J44.DO, Q29.3, R114.1, U34.~D22, U34.~D6
- removed net MISO5: J53.DO, Q35.3, R138.1, U42.~D22, U42.~D6
- removed net MISO6: J62.DO, Q41.3, R162.1, U50.~D22, U50.~D6
- removed net MISO7: J71.DO, Q47.3, R186.1, U58.~D22, U58.~D6
- removed net MISO8: J80.DO, Q53.3, R210.1, U66.~D22, U66.~D6
- removed net MISO9: J89.DO, Q59.3, R234.1, U74.~D22, U74.~D6
- removed net MOSI: J6.DI, Q3.3, U8.D7
- removed net MOSI1: J17.DI, Q5.3, U6.D7
- removed net MOSI10: J98.DI, Q62.3, U82.D7
- removed net MOSI11: J107.DI, Q68.3, U90.D7
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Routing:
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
